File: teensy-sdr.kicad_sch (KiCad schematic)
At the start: 1 part, among them U1 Teensy4.0

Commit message: idk what i am doin
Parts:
- added C1: 22nF, Capacitor_SMD:C_0805_2012Metric_Pad1.18x1.45mm_HandSolder, symbol Device:C
- added C10, C5, C6: 1uF, Capacitor_SMD:C_0805_2012Metric_Pad1.18x1.45mm_HandSolder, symbol Device:C
- added C11, C14, C4: 100nF, Capacitor_SMD:C_0805_2012Metric_Pad1.18x1.45mm_HandSolder, symbol Device:C
- added C12, C13, C17, C7, C8: 2.2uF, Capacitor_SMD:C_0805_2012Metric_Pad1.18x1.45mm_HandSolder, symbol Device:C
- added C15, C16: 100uF, Capacitor_THT:CP_Radial_D8.0mm_P3.50mm, symbol Device:C_Polarized
- added C2: 1nF, Capacitor_SMD:C_0805_2012Metric_Pad1.18x1.45mm_HandSolder, symbol Device:C
- added C3: 10uF, Capacitor_SMD:C_0805_2012Metric_Pad1.18x1.45mm_HandSolder, symbol Device:C
- added C9: 2pF, Capacitor_SMD:C_0805_2012Metric_Pad1.18x1.45mm_HandSolder, symbol Device:C
- added D1: LL4148, Diode_SMD:D_MiniMELF, symbol Diode:LL4148
- added FB3, FB4, FB5, FB6: 2.5k/100M, Inductor_SMD:L_0805_2012Metric_Pad1.05x1.20mm_HandSolder, symbol Device:FerriteBead
- added J1: Conn_Coaxial, Connector_Coaxial:SMA_Molex_73251-1153_EdgeMount_Horizontal, symbol Connector:Conn_Coaxial
- added J2: Battery, Connector_JST:JST_PH_B2B-PH-K_1x02_P2.00mm_Vertical, symbol Connector:Conn_01x02_Pin
- added J3: AudioJack3_SwitchT, Connector_Audio:Jack_3.5mm_CUI_SJ-3524-SMT_Horizontal, symbol Connector_Audio:AudioJack3_SwitchT
- added J4: USB_C_Receptacle_USB2.0_16P, Connector_USB:USB_C_Receptacle_GCT_USB4105-xx-A_16P_TopMnt_Horizontal, symbol Connector:USB_C_Receptacle_USB2.0_16P
- added L1: L, Inductor_SMD:L_10.4x10.4_H4.8, symbol Device:L
- added OLED1: ~, teensy-sdr:Untitled, symbol teensy-sdr:SH1106_FPC
- added R1: 600R, Resistor_SMD:R_0805_2012Metric_Pad1.20x1.40mm_HandSolder, symbol Device:R
- added R10, R8, R9: 4.7k, Resistor_SMD:R_0805_2012Metric_Pad1.20x1.40mm_HandSolder, symbol Device:R
- added R11, R13, R14, R20, R21, R5, R6, R7: 10k, Resistor_SMD:R_0805_2012Metric_Pad1.20x1.40mm_HandSolder, symbol Device:R
- added R12, R23: 100k, Resistor_SMD:R_0805_2012Metric_Pad1.20x1.40mm_HandSolder, symbol Device:R
- added R15: 1.2k, Resistor_SMD:R_0805_2012Metric_Pad1.20x1.40mm_HandSolder, symbol Device:R
- added R16, R17: 5.1k, Resistor_SMD:R_0805_2012Metric_Pad1.20x1.40mm_HandSolder, symbol Device:R
- added R18: 180k, Resistor_SMD:R_0805_2012Metric_Pad1.20x1.40mm_HandSolder, symbol Device:R
- added R19: 20k, Resistor_SMD:R_0805_2012Metric_Pad1.20x1.40mm_HandSolder, symbol Device:R
- added R2, R3: 2k, Resistor_SMD:R_0805_2012Metric_Pad1.20x1.40mm_HandSolder, symbol Device:R
- added R22: 68k, Resistor_SMD:R_0805_2012Metric_Pad1.20x1.40mm_HandSolder, symbol Device:R
- added R4: 560k, Resistor_SMD:R_0805_2012Metric_Pad1.20x1.40mm_HandSolder, symbol Device:R
- added SW1: MSK-12C02 SPDT, PCM_marbastlib-various:SW_MSK12C02-HB, symbol Switch:SW_SPDT
- added SW2, SW3: ~, Rotary_Encoder:RotaryEncoder_Alps_EC11E-Switch_Vertical_H20mm_MountingHoles, symbol Device:RotaryEncoder_Switch_MP
- added U2: Si4735-D60-GU, Package_SO:SSOP-24_3.9x8.7mm_P0.635mm, symbol RF_AM_FM:Si4735-D60-GU
- added U3: AS179-92LF, Package_TO_SOT_SMD:SOT-363_SC-70-6, symbol RF_Switch:AS179-92LF
- added U4, U8: SN74LVC1G14DBV, Package_TO_SOT_SMD:SOT-23-5, symbol 74xGxx:SN74LVC1G14DBV
- added U5: TPS63030DSK, Package_SON:WSON-10-1EP_2.5x2.5mm_P0.5mm_EP1.2x2mm, symbol Regulator_Switching:TPS63030DSK
- added U6: TP4056-42-ESOP8, Package_SO:SOIC-8-1EP_3.9x4.9mm_P1.27mm_EP2.41x3.3mm_ThermalVias, symbol Battery_Management:TP4056-42-ESOP8
- added U7: TLV320AIC23BPW, Package_SO:TSSOP-28_4.4x9.7mm_P0.65mm, symbol Audio:TLV320AIC23BPW
- added Y1: SG-3030CM, Oscillator:Oscillator_SMD_SeikoEpson_SG3030CM, symbol Oscillator:SG-3030CM
- U1: footprint teensy:Teensy40 -> teensy:Teensy40_SMT
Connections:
- net GND: now reaches U1.1 (GND)
- net GND: now also U1.32 (GND), C10.1, C11.1, C12.1, C13.2, C14.2, C17.2, C3.1, C4.1, C7.1, C8.1, C9.1, FB4.1, J1.2 (Ext), J2.1 (Pin_1), J4.A1 (GND), J4.A12 (GND), J4.B1 (GND), J4.B12 (GND), J4.S1 (SHIELD), OLED1.1 (NC_1), OLED1.10 (BS0), OLED1.11 (BS1), OLED1.12 (BS2), OLED1.16 (R/W), OLED1.17 (E/RD), OLED1.21 (D3), OLED1.22 (D4), OLED1.23 (D5), OLED1.24 (D6), OLED1.25 (D7), OLED1.29 (VLSS), OLED1.30 (NC_3), OLED1.7 (NC_2), OLED1.8 (VSS), R15.2, R16.2, R17.2, R19.2, R20.2, R21.1, R23.1, R4.1, R5.2, SW2.C, SW2.MP, SW2.S2, SW3.C, SW3.MP, SW3.S2, U2.13 (GND), U2.14 (GND), U2.4 (GPO2/[~{INT}]), U2.5 (GPO1), U2.9 (RFGND), U3.2 (GND), U4.3 (GND), U5.11 (PGND), U5.3 (PGND), U5.9 (GND), U6.1 (TEMP), U6.3 (GND), U6.9 (EPAD), U7.11 (HPGND), U7.15 (AGND), U7.28 (DGND), U8.3 (GND), Y1.2 (GND)
- net AMP_DIN: now reaches U1.10 (8_TX2_IN1)
- net AMP_DIN: now also U7.4 (DIN)
- net at U1.11 (9_OUT1C): now also SW2.S1
- net at U1.12 (10_CS_MQSR): now also SW3.S1
- net AMP_MOSI: now reaches U1.13 (11_MOSI_CTX1)
- net AMP_MOSI: now also OLED1.19 (D1), R9.1, U2.18 (SDIO), U7.23 (SDIN)
- net AMP_SCLK: now reaches U1.20 (13_SCK_CRX1_LED)
- net AMP_SCLK: now also OLED1.18 (D0), R10.1, U2.17 (SCLK), U7.24 (SCLK)
- net BAT_CHRG: now reaches U1.21 (14_A0_TX3_SPDIF_OUT)
- net BAT_CHRG: now also R13.2, U6.7 (~{CHRG})
- net at U1.22 (15_A1_RX3_SPDIF_IN): now also SW3.A
- net at U1.23 (16_A2_RX4_SCL1): now also SW3.B
- net at U1.24 (17_A3_TX4_SDA1): now also SW2.A
- net at U1.25 (18_A4_SDA0): now also SW2.B
- net BAT_VOLT: now reaches U1.26 (19_A5_SCL0)
- net BAT_VOLT: now also R22.1, R23.2
- net AMP_LRCLK: now reaches U1.27 (20_A6_TX5_LRCLK1)
- net AMP_LRCLK: now also C9.2, R2.2, U7.5 (LRCIN)
- net AMP_BCLK: now reaches U1.28 (21_A7_RX5_BCLK1)
- net AMP_BCLK: now also R3.1, U7.3 (BCLK)
- net AMP_MCLK: now reaches U1.30 (23_A9_CRX1_MCLK1)
- net AMP_MCLK: now also U7.25 (XTI/MCK)
- net +3V3: now reaches U1.31 (3V3)
- net +3V3: now also C1.1, C11.2, C12.2, C4.2, OLED1.6 (VBAT), OLED1.9 (VDD), R10.2, R11.1, R12.1, R6.1, R7.1, R8.2, R9.2, U2.20 (VD), U2.21 (VA), U4.5 (VCC), U7.1 (BVDD), U7.14 (AVDD), U7.22 (MODE), U7.27 (DVDD), U7.8 (HPVDD), U8.5 (VCC), Y1.1 (VIO), Y1.4 (Vcc)
- net VIN: now reaches U1.33 (VIN)
- net VIN: now also C17.1, R18.1, U5.1 (VOUT)
- net JACK_DETECT: now reaches U1.4 (2_OUT2)
- net JACK_DETECT: now also U8.4
- net OLED_D/C: now reaches U1.5 (3_LRCLK2)
- net OLED_D/C: now also OLED1.15 (D/C)
- net D-: now reaches U1.53 (D-)
- net D-: now also J4.A7 (D-), J4.B7 (D-)
- net D+: now reaches U1.54 (D+)
- net D+: now also J4.A6 (D+), J4.B6 (D+)
- net OLED_CS: now reaches U1.6 (4_BCLK2)
- net OLED_CS: now also OLED1.13 (CS)
- net AMP_CS: now reaches U1.7 (5_IN2)
- net AMP_CS: now also R11.2, U7.21 (~{CS})
- net SDR_CS: now reaches U1.8 (6_OUT1D)
- net SDR_CS: now also R7.2, U2.16 (~{SEN})
- net SDR_DOUT: now reaches U1.9 (7_RX2_OUT1A)
- net SDR_DOUT: now also R1.2
- new net: D1.1 (K), U8.2
- new net: D1.2 (A), FB6.1, R12.2
- new net: C14.1, U5.6 (EN), U5.7 (PS/SYNC), U5.8 (VINA)
- new net: R15.1, U6.2 (PROG)
- new net: C13.1, J4.A4 (VBUS), J4.A9 (VBUS), J4.B4 (VBUS), J4.B9 (VBUS), R13.1, R14.1, SW1.1 (A), U6.4 (V_{CC}), U6.8 (CE)
- new net: J2.2 (Pin_2), SW1.3 (C), U6.5 (BAT)
- new net: J1.1 (In), U3.1 (J3)
- new net: R1.1, U2.1 (DOUT)
- new net: R6.2, U2.15 (~{RST})
- new net: U2.19 (RCLK), Y1.3 (OUT)
- new net: R2.1, U2.2 (DFS)
- new net: C1.2, U2.22 (DBYP)
- new net: R3.2, U2.3 (GPO3/[DCLK])
- new net: C2.1, U2.8 (FMI)
- new net: R18.2, R19.1, U5.10 (FB)
- new net: R22.2, SW1.2 (B), U5.5 (VIN)
- new net: C3.2, OLED1.14 (RES), R8.1
- new net: C15.2, FB5.1, R20.1
- new net: FB5.2, J3.T
- new net: C16.2, FB3.1, R21.2
- new net: FB3.2, J3.R
- new net: OLED1.26 (IREF), R4.2
- new net: C2.2, U3.5 (J1)
- new net: C16.1, U7.10 (RHPOUT)
- new net: C15.1, U7.9 (LHPOUT)
- new net: L1.1, U5.2 (L2)
- new net: L1.2, U5.4 (L1)
- new net: J4.B5 (CC2), R16.1
- new net: FB6.2, J3.TN
- new net: J4.A5 (CC1), R17.1
- new net: C5.1, OLED1.3 (C2N)
- new net: C5.2, OLED1.2 (C2P)
- new net: U3.6 (V2), U4.4
- new net: C10.2, C8.2, OLED1.28 (VCC)
- new net: C7.2, OLED1.27 (VCOMH)
- new net: C6.1, OLED1.5 (C1N)
- new net: C6.2, OLED1.4 (C1P)
- new net BAT_STDBY: R14.2, U6.6 (~{STDBY})
- new net JACK_ANT: FB4.2, J3.S, U3.3 (J2)
- new net RF_SWITCH: R5.1, U3.4 (V1), U4.2
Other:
- note added: "5V? Who knows"
- note added: "Audio Signal on T means we gotta filter that out :/"
- note added: "Bypass battery when off for USB-Only Power"
- note added: "Fancy antenna switching"
- note added: "GPO1 & GPO2 LOW For SPI-Like 3-Wire"
- note added: "Gonna suck to solder but fuck it we ball"
- note added: "MODE High For SPI-Like 3-Wire"
- note added: "Optional for USB comunication via the USB-C connector"
- note added: "RF Isolation From Audio Driver For Headphone Antenna"
- note added: "The holy knob TWICE"
- note added: "Voltage Divider for Voltage measuring"
- moved on the sheet: U1

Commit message: PCB Refractor
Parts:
- C1: LCSC (none) -> C107147
- C10, C5, C6: LCSC (none) -> C28323
- C11, C14, C4: LCSC (none) -> C49678
- C12, C13, C17, C7, C8: LCSC (none) -> C28234
- C15, C16: LCSC (none) -> C2990945
- C2: LCSC (none) -> C94121
- C3: LCSC (none) -> C15850
- C9: LCSC (none) -> C519932
- D1: LCSC (none) -> C68883
- FB3, FB4, FB5, FB6: LCSC (none) -> C394486
- J1: LCSC (none) -> C5859238
- J2: LCSC (none) -> C20088550
- J3: LCSC (none) -> C22359753
- J4: LCSC (none) -> C3025063
- L1: value L -> 1.5uF; footprint Inductor_SMD:L_10.4x10.4_H4.8 -> Inductor_SMD:L_7.3x7.3_H3.5; LCSC (none) -> C5189745
- R1: value 600R -> 1k; LCSC (none) -> C95781
- R10, R8, R9: LCSC (none) -> C60816
- R11, R13, R14, R20, R21, R5, R6, R7: LCSC (none) -> C84376
- R12, R23: LCSC (none) -> C96346
- R15: LCSC (none) -> C114526
- R16, R17: LCSC (none) -> C2930296
- R18: LCSC (none) -> C17501
- R19: LCSC (none) -> C114566
- R2, R3: LCSC (none) -> C114572
- R22: LCSC (none) -> C17801
- R4: LCSC (none) -> C865557
- SW1: LCSC (none) -> C431540
- SW2, SW3: LCSC (none) -> C1322542
- U2: LCSC (none) -> C17686189
- U3: LCSC (none) -> C83422
- U4, U8: LCSC (none) -> C7835
- U5: LCSC (none) -> C12462
- U6: LCSC (none) -> C16581
- U7: LCSC (none) -> C9915
- Y1: LCSC (none) -> C21058396
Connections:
- net +3V3: now also R13.1, R14.1
- net at C13.1, J4.A4 (VBUS), J4.A9 (VBUS)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: no longer R13.1, R14.1
- no-connect marks 26 -> 47

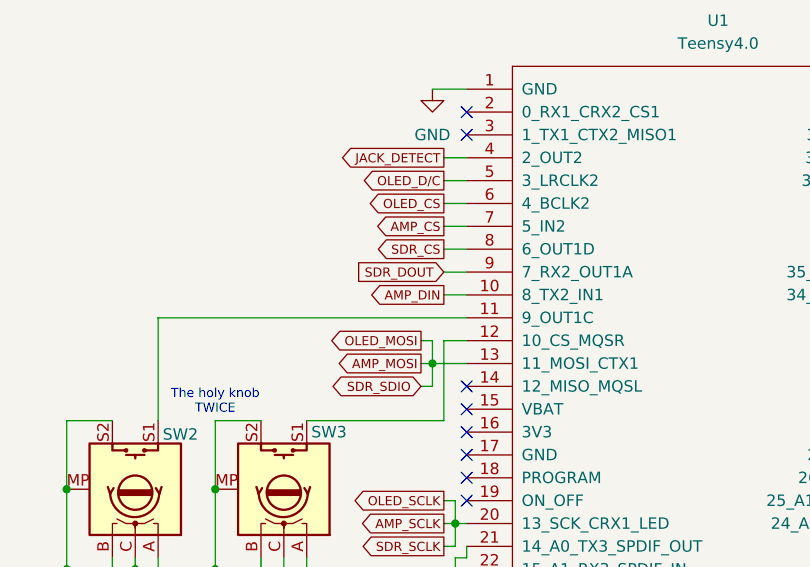
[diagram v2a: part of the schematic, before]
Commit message: fix swapped I2S lines
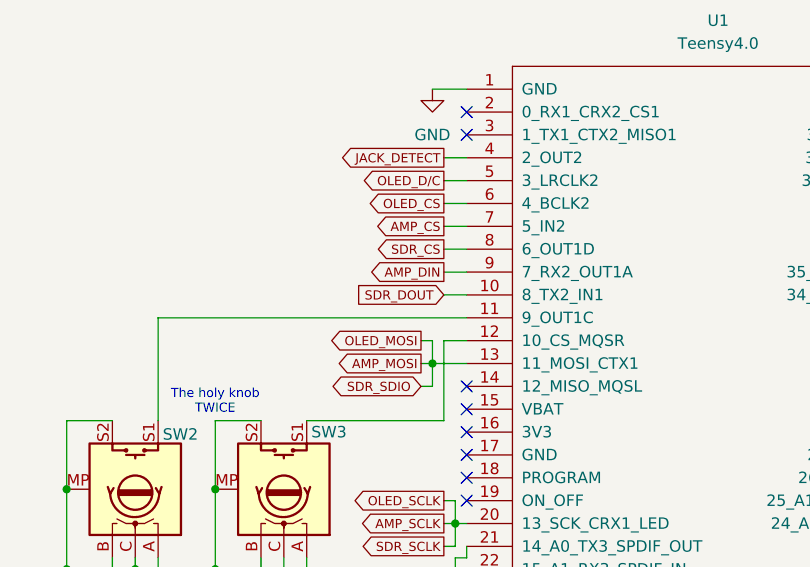
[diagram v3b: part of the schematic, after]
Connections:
- net AMP_DIN: now also U1.9 (7_RX2_OUT1A); no longer U1.10 (8_TX2_IN1)
- net SDR_DOUT: now also U1.10 (8_TX2_IN1); no longer U1.9 (7_RX2_OUT1A)
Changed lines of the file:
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@@
 	(wire
 		(pts
-			(xy 187.96 114.3) (xy 190.5 114.3)
-		)
-		(stroke
-			(width 0)
-			(type default)
-		)
-	)
-	(wire
-		(pts
 			(xy 44.45 199.39) (xy 44.45 212.09)
 		)
@@
 	(wire
 		(pts
-			(xy 190.5 116.84) (xy 187.96 116.84)
-		)
-		(stroke
-			(width 0)
-			(type default)
-		)
-	)
-	(wire
-		(pts
 			(xy 53.34 34.29) (xy 48.26 34.29)
 		)
@@
 	(wire
 		(pts
+			(xy 187.96 116.84) (xy 190.5 116.84)
+		)
+		(stroke
+			(width 0)
+			(type default)
+		)
+	)
+	(wire
+		(pts
 			(xy 156.21 119.38) (xy 190.5 119.38)
 		)
@@
 	(wire
 		(pts
+			(xy 187.96 114.3) (xy 190.5 114.3)
+		)
+		(stroke
+			(width 0)
+			(type default)
+		)
+	)
+	(wire
+		(pts
 			(xy 86.36 38.1) (xy 83.82 38.1)
 		)
@@
 	(global_label "SDR_DOUT"
 		(shape input)
-		(at 187.96 114.3 180)
+		(at 187.96 116.84 180)
 		(fields_autoplaced yes)
 		(effects
@@
 		)
 		(property "Intersheetrefs" "${INTERSHEET_REFS}"
-			(at 177.8795 114.3 0)
+			(at 177.8795 116.84 0)
 			(effects
 				(font
@@
 	(global_label "AMP_DIN"
 		(shape output)
-		(at 187.96 116.84 180)
+		(at 187.96 114.3 180)
 		(fields_autoplaced yes)
 		(effects
@@
 		)
 		(property "Intersheetrefs" "${INTERSHEET_REFS}"
-			(at 179.1858 116.84 0)
+			(at 179.1858 114.3 0)
 			(effects
 				(font
